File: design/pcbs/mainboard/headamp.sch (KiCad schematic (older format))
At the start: 26 parts, among them U7 OPA1612AxD, U8 LME49600, U9 LME49600

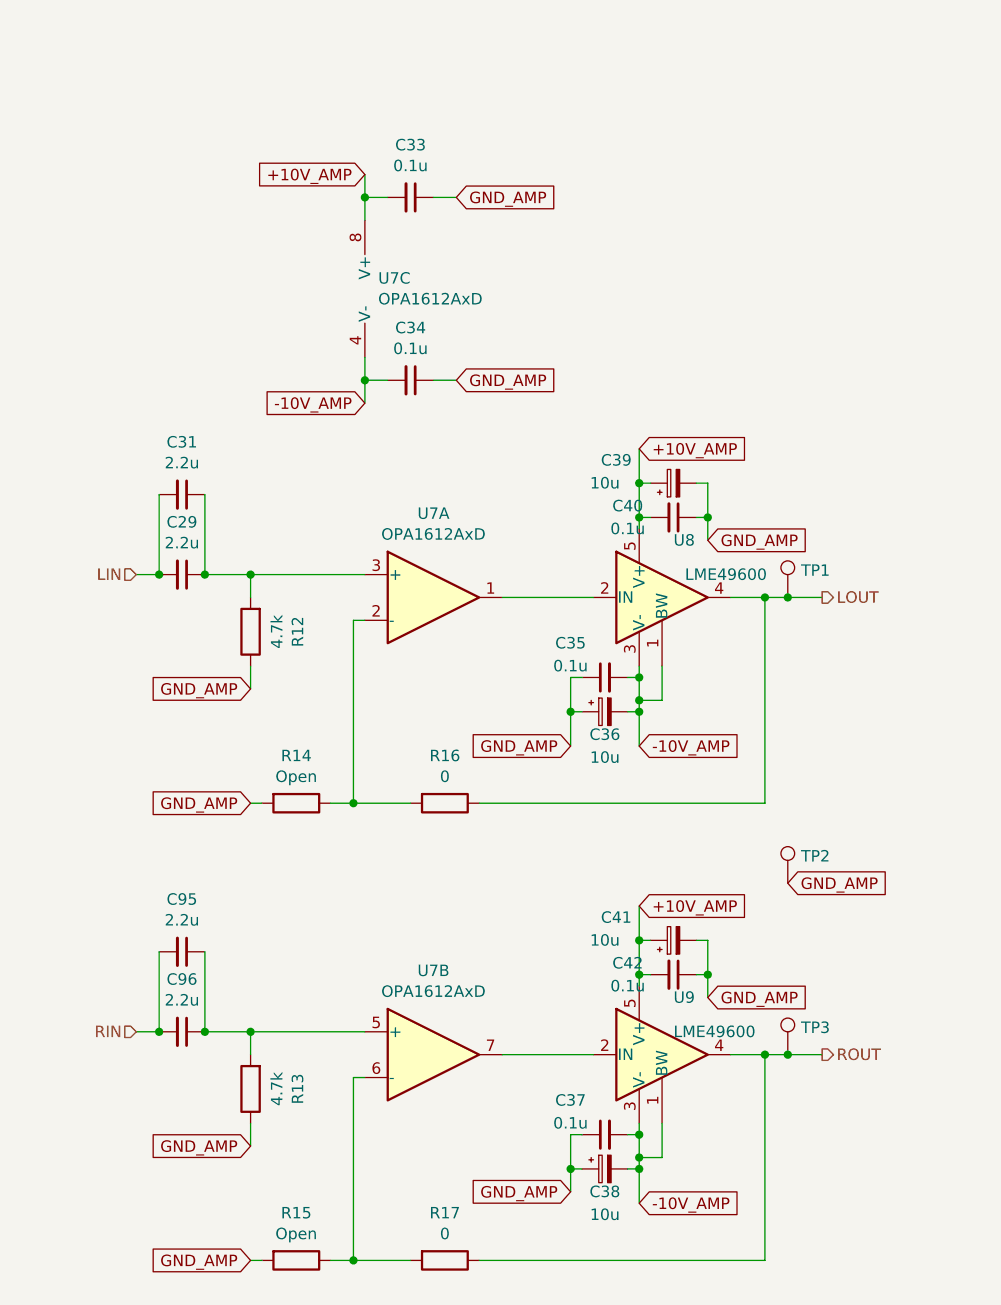
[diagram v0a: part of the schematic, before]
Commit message: Renumbered footprints to follow board position.
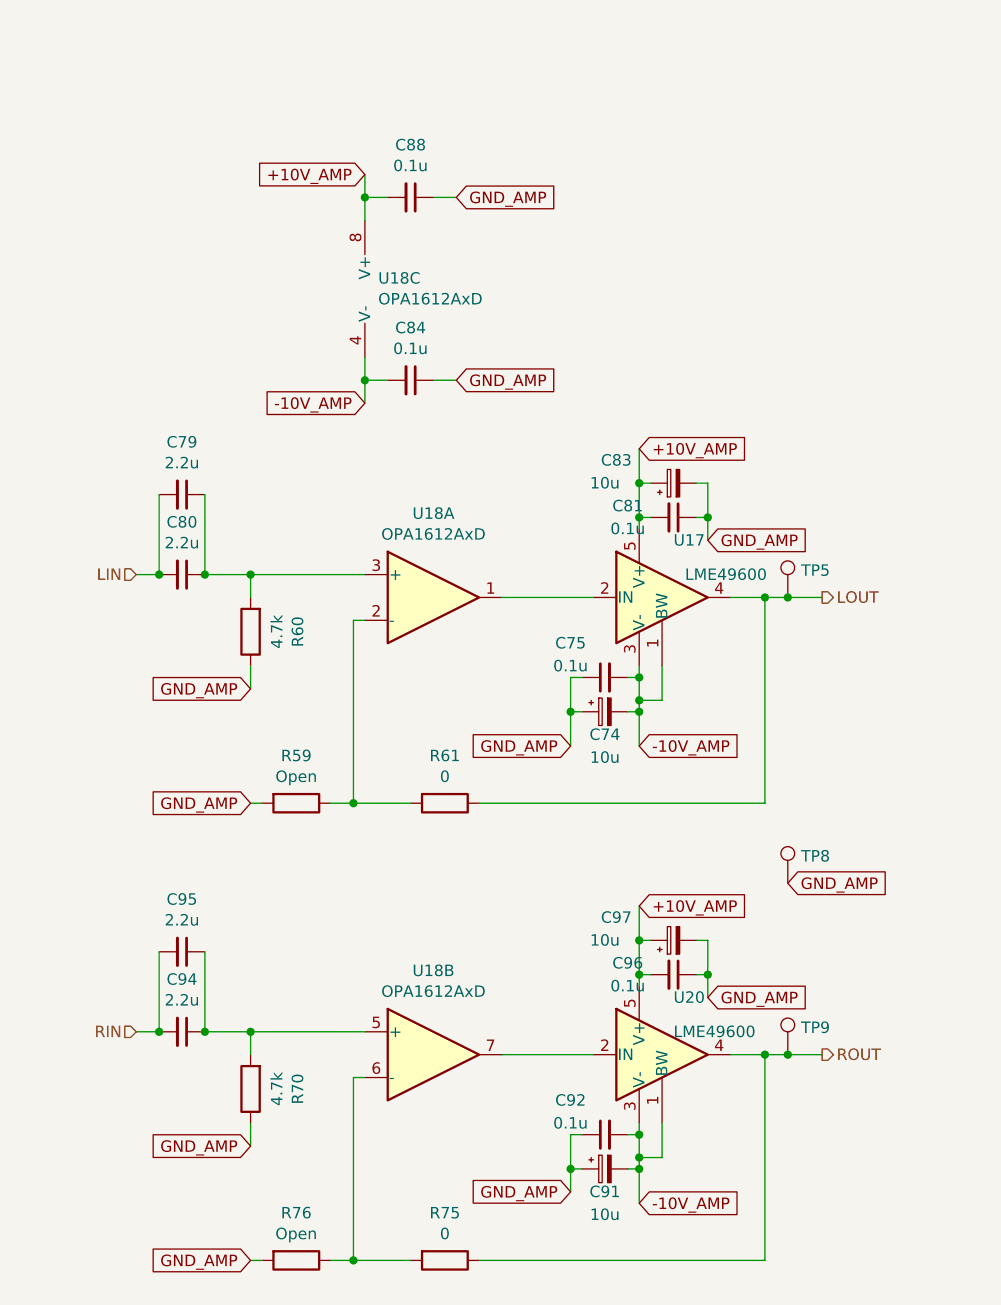
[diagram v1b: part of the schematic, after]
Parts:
- renumbered C36 to C74, C35 to C75, C31 to C79, C29 to C80, C40 to C81, C39 to C83, C34 to C84, C33 to C88, C38 to C91, C37 to C92, C96 to C94, C42 to C96, C41 to C97, R14 to R59, R12 to R60, R16 to R61, R13 to R70, R17 to R75, R15 to R76, TP1 to TP5, TP2 to TP8, TP3 to TP9, U8 to U17, U7 to U18, U9 to U20
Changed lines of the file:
@@
 AKG K701 specs:\n62 ohm\n200 mW max\n105 dB SPL/V (3.56 Pa rel to 20 uPa @ 1 V)\n\n=> Imax 57 mA RMS, Vmax 3.5 V RMS\n=> max volume (at 200 mW) 116 dB\n\n1.3 Vrms as output by DAC I2V stage will give 107 dB,\nthis is fine.  Therefore just a buffer stage required.\n\nJumpers added to enable gain increase if high Z cans are used.
 $Comp
-L Amplifier_Audio:LME49600 U8
+L Amplifier_Audio:LME49600 U17
 U 1 1 5EC7A59F
 P 5300 3100
-F 0 "U8" H 5350 3350 50  0000 L CNN
+F 0 "U17" H 5350 3350 50  0000 L CNN
 F 1 "LME49600" H 5400 3200 50  0000 L CNN
 F 2 "Package_TO_SOT_SMD:TO-263-5_TabPin3" H 5300 3100 50  0001 C CIN
@@
 $EndComp
 $Comp
-L Amplifier_Audio:LME49600 U9
+L Amplifier_Audio:LME49600 U20
 U 1 1 5EC7AD17
 P 5300 5100
-F 0 "U9" H 5350 5350 50  0000 L CNN
+F 0 "U20" H 5350 5350 50  0000 L CNN
 F 1 "LME49600" H 5350 5200 50  0000 L CNN
 F 2 "Package_TO_SOT_SMD:TO-263-5_TabPin3" H 5300 5100 50  0001 C CIN
@@
 $EndComp
 $Comp
-L Amplifier_Operational:OPA1612AxD U7
+L Amplifier_Operational:OPA1612AxD U18
 U 1 1 5EC7D37B
 P 4300 3100
-F 0 "U7" H 4300 3467 50  0000 C CNN
+F 0 "U18" H 4300 3467 50  0000 C CNN
 F 1 "OPA1612AxD" H 4300 3376 50  0000 C CNN
 F 2 "Package_SO:SOIC-8_3.9x4.9mm_P1.27mm" H 4300 3100 50  0001 C CNN
@@
 $EndComp
 $Comp
-L Amplifier_Operational:OPA1612AxD U7
+L Amplifier_Operational:OPA1612AxD U18
 U 2 1 5EC7E916
 P 4300 5100
-F 0 "U7" H 4300 5467 50  0000 C CNN
+F 0 "U18" H 4300 5467 50  0000 C CNN
 F 1 "OPA1612AxD" H 4300 5376 50  0000 C CNN
 F 2 "Package_SO:SOIC-8_3.9x4.9mm_P1.27mm" H 4300 5100 50  0001 C CNN
@@
 $EndComp
 $Comp
-L Amplifier_Operational:OPA1612AxD U7
+L Amplifier_Operational:OPA1612AxD U18
 U 3 1 5EC7F6FB
 P 4100 1750
-F 0 "U7" H 4058 1796 50  0000 L CNN
+F 0 "U18" H 4058 1796 50  0000 L CNN
 F 1 "OPA1612AxD" H 4058 1705 50  0000 L CNN
 F 2 "Package_SO:SOIC-8_3.9x4.9mm_P1.27mm" H 4100 1750 50  0001 C CNN
@@
 	4000 5200 3950 5200
 $Comp
-L Device:C_Small C34
+L Device:C_Small C84
 U 1 1 5EC8CA29
 P 4200 2150
-F 0 "C34" V 3971 2150 50  0000 C CNN
+F 0 "C84" V 3971 2150 50  0000 C CNN
 F 1 "0.1u" V 4062 2150 50  0000 C CNN
 F 2 "Capacitor_SMD:C_0603_1608Metric" H 4200 2150 50  0001 C CNN
@@
 $EndComp
 $Comp
-L Device:C_Small C33
+L Device:C_Small C88
 U 1 1 5EC8DF3F
 P 4200 1350
-F 0 "C33" V 3971 1350 50  0000 C CNN
+F 0 "C88" V 3971 1350 50  0000 C CNN
 F 1 "0.1u" V 4062 1350 50  0000 C CNN
 F 2 "Capacitor_SMD:C_0603_1608Metric" H 4200 1350 50  0001 C CNN
@@
 	3000 3000 3100 3000
 $Comp
-L Device:C_Small C40
+L Device:C_Small C81
 U 1 1 5EC954F1
 P 5350 2750
-F 0 "C40" V 5300 2550 50  0000 C CNN
+F 0 "C81" V 5300 2550 50  0000 C CNN
 F 1 "0.1u" V 5400 2550 50  0000 C CNN
 F 2 "Capacitor_SMD:C_0603_1608Metric" H 5350 2750 50  0001 C CNN
@@
 $EndComp
 $Comp
-L Device:CP_Small C39
+L Device:CP_Small C83
 U 1 1 5EC95EA4
 P 5350 2600
-F 0 "C39" V 5450 2850 50  0000 C CNN
+F 0 "C83" V 5450 2850 50  0000 C CNN
 F 1 "10u" V 5350 2900 50  0000 C CNN
 F 2 "Capacitor_Tantalum_SMD:CP_EIA-3216-18_Kemet-A" H 5350 2600 50  0001 C CNN
@@
 	5200 2600 5200 2750
 $Comp
-L Device:C_Small C42
+L Device:C_Small C96
 U 1 1 5EC9BF61
 P 5350 4750
-F 0 "C42" V 5300 4550 50  0000 C CNN
+F 0 "C96" V 5300 4550 50  0000 C CNN
 F 1 "0.1u" V 5400 4550 50  0000 C CNN
 F 2 "Capacitor_SMD:C_0603_1608Metric" H 5350 4750 50  0001 C CNN
@@
 $EndComp
 $Comp
-L Device:CP_Small C41
+L Device:CP_Small C97
 U 1 1 5EC9BF6B
 P 5350 4600
-F 0 "C41" V 5450 4850 50  0000 C CNN
+F 0 "C97" V 5450 4850 50  0000 C CNN
 F 1 "10u" V 5350 4900 50  0000 C CNN
 F 2 "Capacitor_Tantalum_SMD:CP_EIA-3216-18_Kemet-A" H 5350 4600 50  0001 C CNN
@@
 	5750 3100 5750 4000
 $Comp
-L Device:C_Small C35
+L Device:C_Small C75
 U 1 1 5ECAA82E
 P 5050 3450
-F 0 "C35" V 5200 3600 50  0000 C CNN
+F 0 "C75" V 5200 3600 50  0000 C CNN
 F 1 "0.1u" V 5100 3600 50  0000 C CNN
 F 2 "Capacitor_SMD:C_0603_1608Metric" H 5050 3450 50  0001 C CNN
@@
 $EndComp
 $Comp
-L Device:CP_Small C36
+L Device:CP_Small C74
 U 1 1 5ECAA838
 P 5050 3600
-F 0 "C36" V 5150 3600 50  0000 C CNN
+F 0 "C74" V 5150 3600 50  0000 C CNN
 F 1 "10u" V 5250 3600 50  0000 C CNN
 F 2 "Capacitor_Tantalum_SMD:CP_EIA-3216-18_Kemet-A" H 5050 3600 50  0001 C CNN
@@
 	5200 3600 5200 3550
 $Comp
-L Device:C_Small C37
+L Device:C_Small C92
 U 1 1 5ECBA7A4
 P 5050 5450
-F 0 "C37" V 5200 5600 50  0000 C CNN
+F 0 "C92" V 5200 5600 50  0000 C CNN
 F 1 "0.1u" V 5100 5600 50  0000 C CNN
 F 2 "Capacitor_SMD:C_0603_1608Metric" H 5050 5450 50  0001 C CNN
@@
 $EndComp
 $Comp
-L Device:CP_Small C38
+L Device:CP_Small C91
 U 1 1 5ECBA7AE
 P 5050 5600
-F 0 "C38" V 5150 5600 50  0000 C CNN
+F 0 "C91" V 5150 5600 50  0000 C CNN
 F 1 "10u" V 5250 5600 50  0000 C CNN
 F 2 "Capacitor_Tantalum_SMD:CP_EIA-3216-18_Kemet-A" H 5050 5600 50  0001 C CNN
@@
 Connection ~ 3950 4000
 $Comp
-L Device:R R14
+L Device:R R59
 U 1 1 5ED2BE16
 P 3700 4000
-F 0 "R14" V 3493 4000 50  0000 C CNN
+F 0 "R59" V 3493 4000 50  0000 C CNN
 F 1 "Open" V 3584 4000 50  0000 C CNN
 F 2 "Resistor_THT:R_Axial_DIN0207_L6.3mm_D2.5mm_P10.16mm_Horizontal" V 3630 4000 50  0001 C CNN
@@
 $EndComp
 $Comp
-L Device:R R16
+L Device:R R61
 U 1 1 5ED2C3CF
 P 4350 4000
-F 0 "R16" V 4143 4000 50  0000 C CNN
+F 0 "R61" V 4143 4000 50  0000 C CNN
 F 1 "0" V 4234 4000 50  0000 C CNN
 F 2 "Resistor_THT:R_Axial_DIN0207_L6.3mm_D2.5mm_P10.16mm_Horizontal" V 4280 4000 50  0001 C CNN
@@
 $EndComp
 $Comp
-L Device:R R17
+L Device:R R75
 U 1 1 5ED2CE5E
 P 4350 6000
-F 0 "R17" V 4143 6000 50  0000 C CNN
+F 0 "R75" V 4143 6000 50  0000 C CNN
 F 1 "0" V 4234 6000 50  0000 C CNN
 F 2 "Resistor_THT:R_Axial_DIN0207_L6.3mm_D2.5mm_P10.16mm_Horizontal" V 4280 6000 50  0001 C CNN
@@
 $EndComp
 $Comp
-L Device:R R15
+L Device:R R76
 U 1 1 5ED2DA9F
 P 3700 6000
-F 0 "R15" V 3493 6000 50  0000 C CNN
+F 0 "R76" V 3493 6000 50  0000 C CNN
 F 1 "Open" V 3584 6000 50  0000 C CNN
 F 2 "Resistor_THT:R_Axial_DIN0207_L6.3mm_D2.5mm_P10.16mm_Horizontal" V 3630 6000 50  0001 C CNN
@@
 	4500 6000 5750 6000
 $Comp
-L Device:R R12
+L Device:R R60
 U 1 1 5ED747C1
 P 3500 3250
-F 0 "R12" V 3293 3250 50  0000 C CNN
+F 0 "R60" V 3293 3250 50  0000 C CNN
 F 1 "4.7k" V 3384 3250 50  0000 C CNN
 F 2 "Resistor_SMD:R_0603_1608Metric" V 3430 3250 50  0001 C CNN
@@
 Note potential offset voltage of up \nto 1.2 mV due to 4.7 k resistor.\nAdding compensatory 4.7 k in feedback\nloop leads to high noise.
 $Comp
-L Device:C_Small C29
+L Device:C_Small C80
 U 1 1 5EDA31C4
 P 3200 3000
-F 0 "C29" V 2971 3000 50  0000 C CNN
+F 0 "C80" V 2971 3000 50  0000 C CNN
 F 1 "2.2u" V 3062 3000 50  0000 C CNN
 F 2 "Capacitor_THT:C_Rect_L18.0mm_W11.0mm_P15.00mm_FKS3_FKP3" H 3200 3000 50  0001 C CNN
@@
 	3300 5000 3500 5000
 $Comp
-L Device:R R13
+L Device:R R70
 U 1 1 5EDAC893
 P 3500 5250
-F 0 "R13" V 3293 5250 50  0000 C CNN
+F 0 "R70" V 3293 5250 50  0000 C CNN
 F 1 "4.7k" V 3384 5250 50  0000 C CNN
 F 2 "Resistor_SMD:R_0603_1608Metric" V 3430 5250 50  0001 C CNN
@@
 Connection ~ 5850 5100
 $Comp
-L Connector:TestPoint TP3
+L Connector:TestPoint TP9
 U 1 1 5ECB40D4
 P 5850 5100
-F 0 "TP3" H 5908 5218 50  0000 L CNN
+F 0 "TP9" H 5908 5218 50  0000 L CNN
 F 1 "TestPoint" H 5908 5127 50  0001 L CNN
 F 2 "TestPoint:TestPoint_THTPad_D3.0mm_Drill1.5mm" H 6050 5100 50  0001 C CNN
@@
 $EndComp
 $Comp
-L Connector:TestPoint TP2
+L Connector:TestPoint TP8
 U 1 1 5ECB4945
 P 5850 4350
-F 0 "TP2" H 5908 4468 50  0000 L CNN
+F 0 "TP8" H 5908 4468 50  0000 L CNN
 F 1 "TestPoint" H 5908 4377 50  0001 L CNN
 F 2 "TestPoint:TestPoint_THTPad_D3.0mm_Drill1.5mm" H 6050 4350 50  0001 C CNN
@@
 Connection ~ 5850 3100
 $Comp
-L Connector:TestPoint TP1
+L Connector:TestPoint TP5
 U 1 1 5ECB35D5
 P 5850 3100
-F 0 "TP1" H 5908 3218 50  0000 L CNN
+F 0 "TP5" H 5908 3218 50  0000 L CNN
 F 1 "TestPoint" H 5908 3127 50  0001 L CNN
 F 2 "TestPoint:TestPoint_THTPad_D3.0mm_Drill1.5mm" H 6050 3100 50  0001 C CNN
@@
 -10V_AMP
 $Comp
-L Device:C_Small C31
+L Device:C_Small C79
 U 1 1 5EDFABAA
 P 3200 2650
-F 0 "C31" V 2971 2650 50  0000 C CNN
+F 0 "C79" V 2971 2650 50  0000 C CNN
 F 1 "2.2u" V 3062 2650 50  0000 C CNN
 F 2 "Capacitor_THT:C_Rect_L18.0mm_W11.0mm_P15.00mm_FKS3_FKP3" H 3200 2650 50  0001 C CNN
@@
 Connection ~ 3300 3000
 $Comp
-L Device:C_Small C96
+L Device:C_Small C94
 U 1 1 5EDFFBDF
 P 3200 5000
-F 0 "C96" V 2971 5000 50  0000 C CNN
+F 0 "C94" V 2971 5000 50  0000 C CNN
 F 1 "2.2u" V 3062 5000 50  0000 C CNN
 F 2 "Capacitor_THT:C_Rect_L18.0mm_W11.0mm_P15.00mm_FKS3_FKP3" H 3200 5000 50  0001 C CNN

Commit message: Fixed title blocks. Added fab outputs.
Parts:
- U18: LCSC (none) -> C94590
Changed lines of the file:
@@
 encoding utf-8
 Sheet 5 10
-Title ""
-Date ""
-Rev ""
-Comp ""
-Comment1 ""
-Comment2 ""
+Title "DAC1 Main board"
+Date "2020-06-27"
+Rev "1.0.0"
+Comp "© Mark Pinese 2020"
+Comment1 "To view a copy of this license, visit https://creativecommons.org/licenses/by/4.0"
+Comment2 "This work is licensed under CC BY 4.0."
 Comment3 ""
 Comment4 ""
@@
 F 4 "296-39098-1-ND" H 4300 3100 50  0001 C CNN "DigiKey"
 F 5 "Yes" H 4300 3100 50  0001 C CNN "Done"
+F 6 "C94590" H 4300 3100 50  0001 C CNN "LCSC"
 	1    4300 3100
 	1    0    0    -1
@@
 F 4 "296-39098-1-ND" H 4300 5100 50  0001 C CNN "DigiKey"
 F 5 "Yes" H 4300 5100 50  0001 C CNN "Done"
+F 6 "C94590" H 4300 5100 50  0001 C CNN "LCSC"
 	2    4300 5100
 	1    0    0    -1
@@
 F 4 "296-39098-1-ND" H 4100 1750 50  0001 C CNN "DigiKey"
 F 5 "Yes" H 4100 1750 50  0001 C CNN "Done"
+F 6 "C94590" H 4100 1750 50  0001 C CNN "LCSC"
 	3    4100 1750
 	1    0    0    -1
